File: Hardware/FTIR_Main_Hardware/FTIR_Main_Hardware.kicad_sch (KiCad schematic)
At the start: 64 parts, among them J1 RJ45_LED_Shielded, Q1 IRF7606PBF, Q2 BSS138, Q3 IRF7606PBF, Q4 BSS138, Q5 IRF7606PBF, Q6 BSS138, U1 Opamp_Dual, U3 OKI, U6 Peensy4.1_DEV-16771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

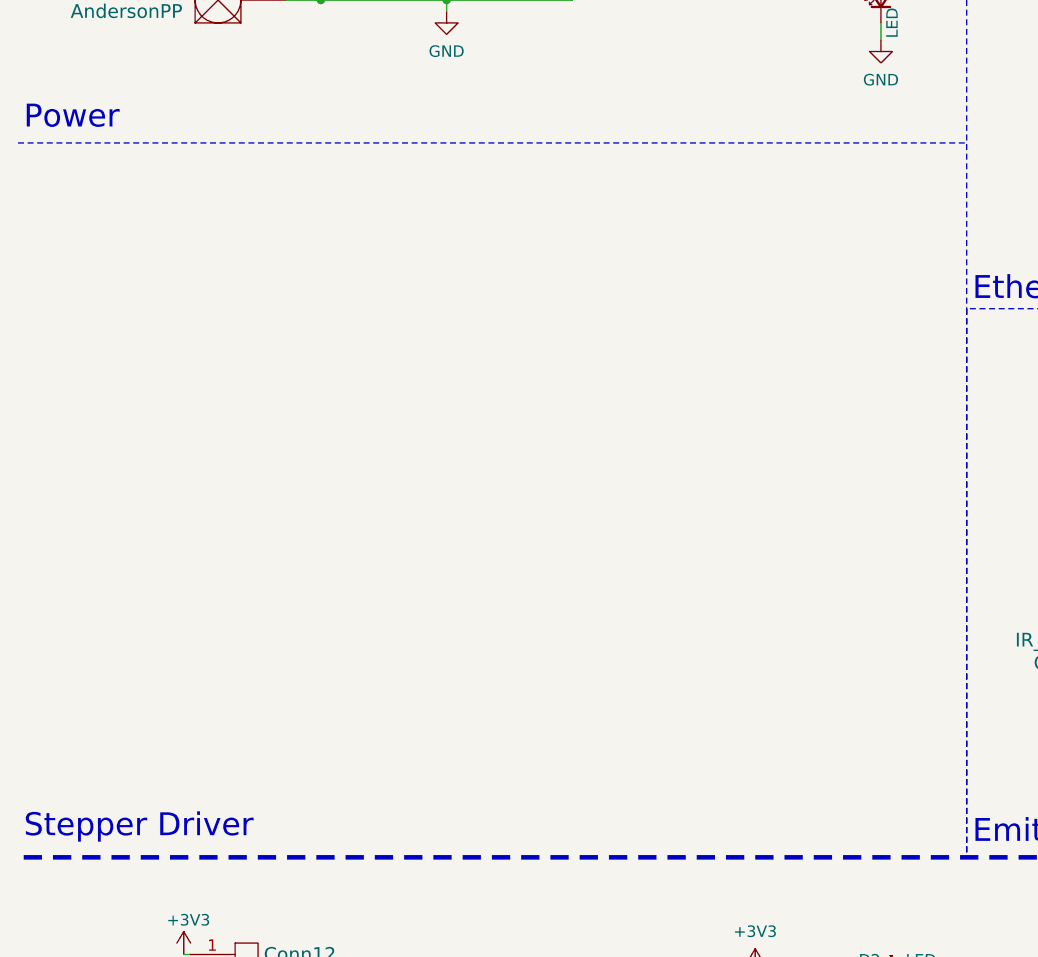
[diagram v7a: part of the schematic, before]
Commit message: Revert "Symbol for stepper"
This reverts commit 3005be89c2a7f566bd27afdf3620319c1e39fccb.
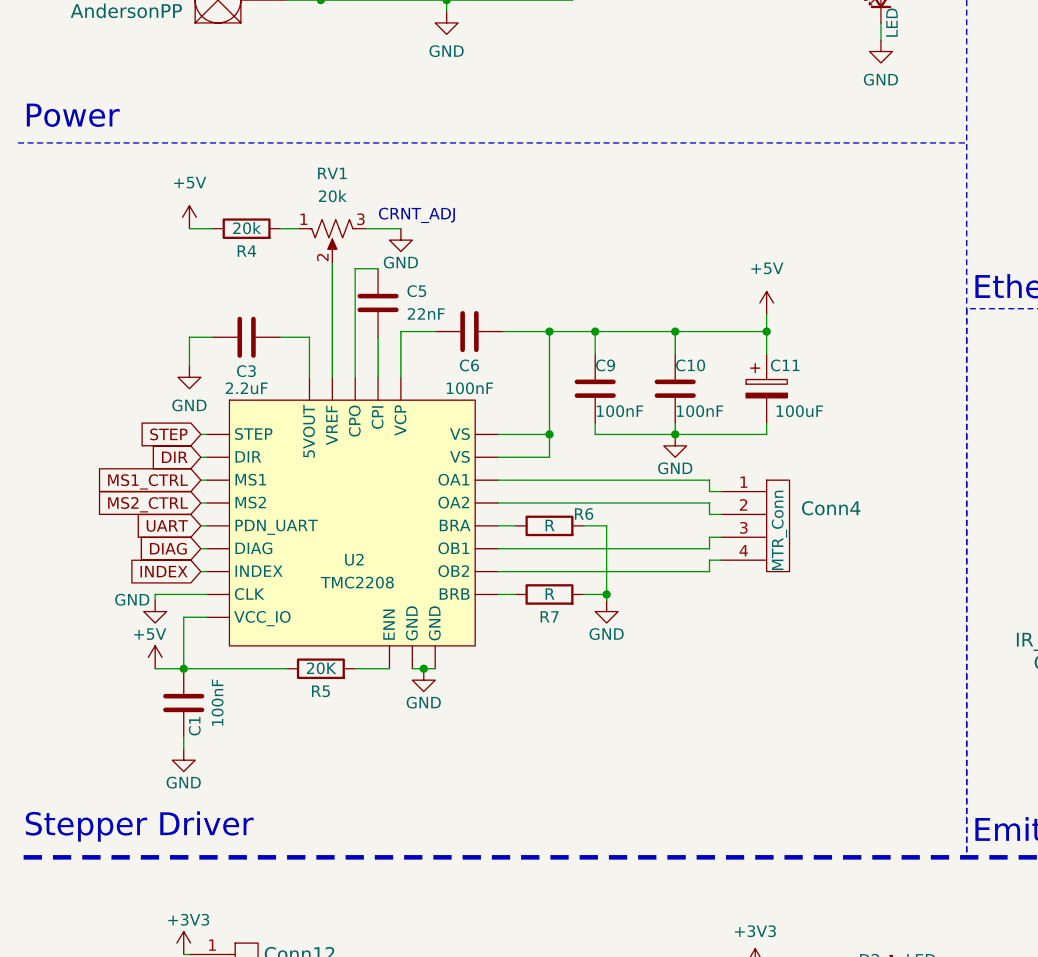
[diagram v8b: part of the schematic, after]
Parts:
- added C1, C10, C6, C9: 100nF, symbol Device:C
- added C11: 100uF, symbol Device:C_Polarized
- added C3: 2.2uF, symbol Device:C
- added C5: 22nF, symbol Device:C
- added Conn4: MTR_Conn, symbol MRDT_Connectors:Molex_SL_04
- added R4: 20k, symbol Device:R
- added R5: 20K, symbol Device:R
- added R6, R7: R, symbol Device:R
- added RV1: 20k, symbol Device:R_Potentiometer_US
- added U2: TMC2208, symbol MRDT_Devices:TMC2208
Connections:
- net +5V: now also C1.1, C10.1, C11.1, C6.2, C9.1, R4.1, R5.1, U2. (VS)
- net DIAG: now also U2. (VS)
- net DIR: now also U2. (VS)
- net GND: now also C1.2, C10.2, C11.2, C3.1, C9.2, R6.2, R7.2, RV1.3, U2. (VS)
- net INDEX: now also U2. (VS)
- net MS1_CTRL: now also U2. (VS)
- net MS2_CTRL: now also U2. (VS)
- net STEP: now also U2. (VS)
- net UART: now also U2. (VS)
- new net: R6.1, U2. (VS)
- new net: R4.2, RV1.1
- new net: C3.2, U2. (VS)
- new net: RV1.2, U2. (VS)
- new net: C5.1, U2. (VS)
- new net: C5.2, U2. (VS)
- new net: Conn4.1, U2. (VS)
- new net: Conn4.2, U2. (VS)
- new net: Conn4.3, U2. (VS)
- new net: Conn4.4, U2. (VS)
- new net: R5.2, U2. (VS)
- new net: R7.1, U2. (VS)
- new net: C6.1, U2. (VS)
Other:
- note added: "CRNT_ADJ"
